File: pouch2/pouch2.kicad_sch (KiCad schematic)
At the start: 7 parts, among them U1 Pico

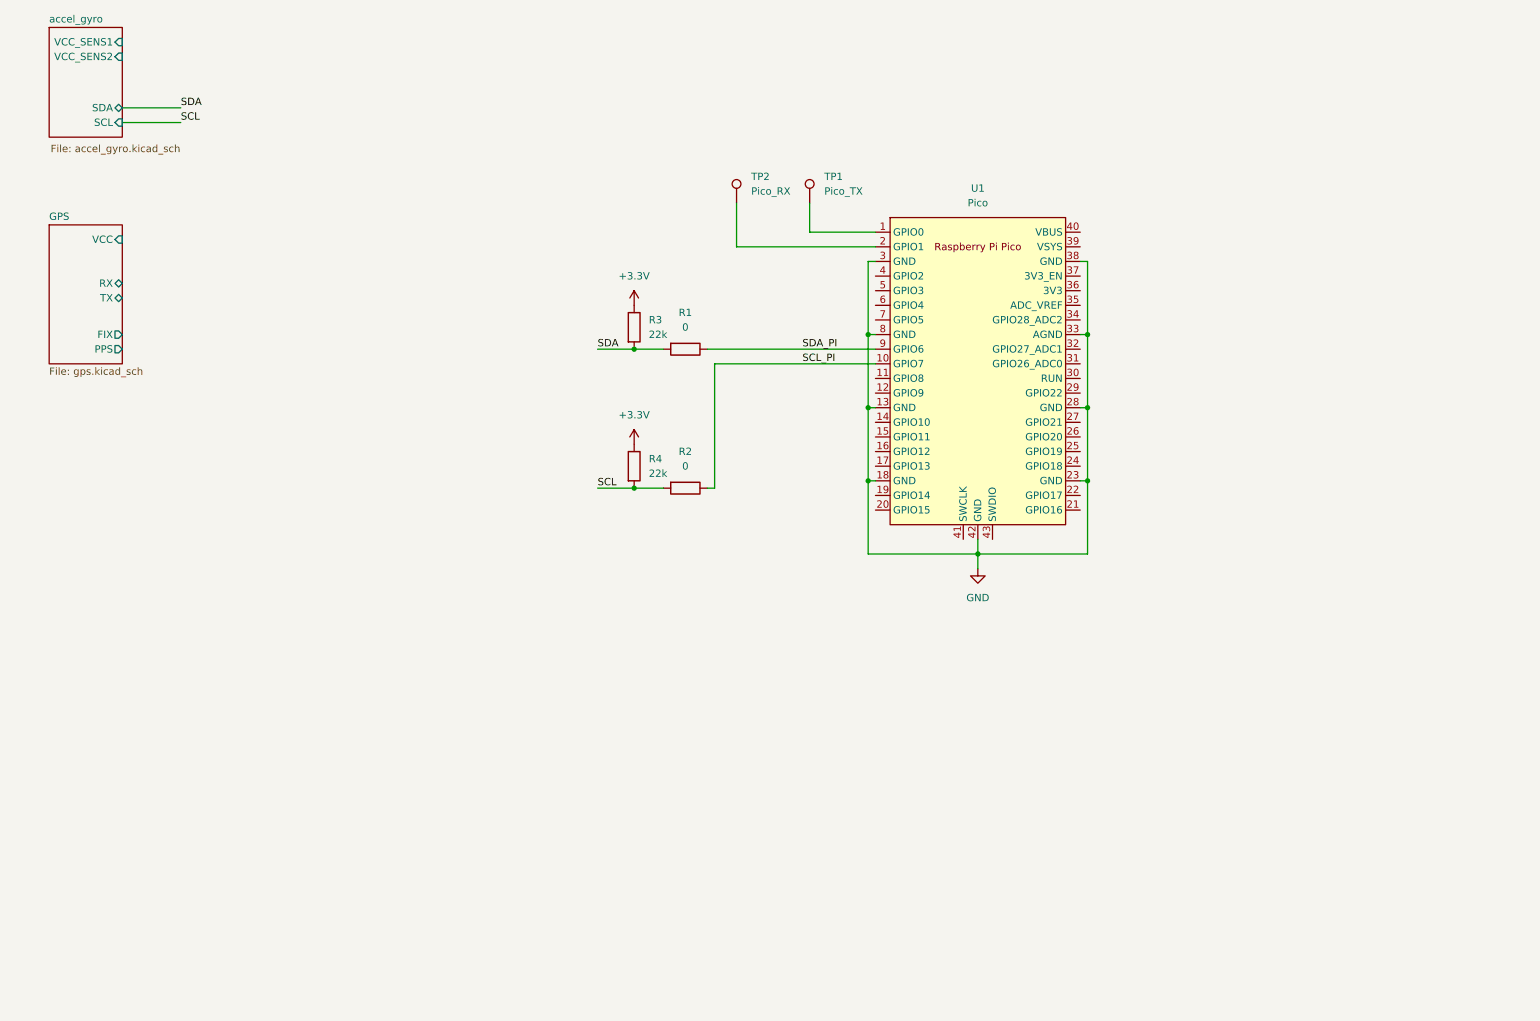
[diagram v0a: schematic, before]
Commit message: added power, sdcard
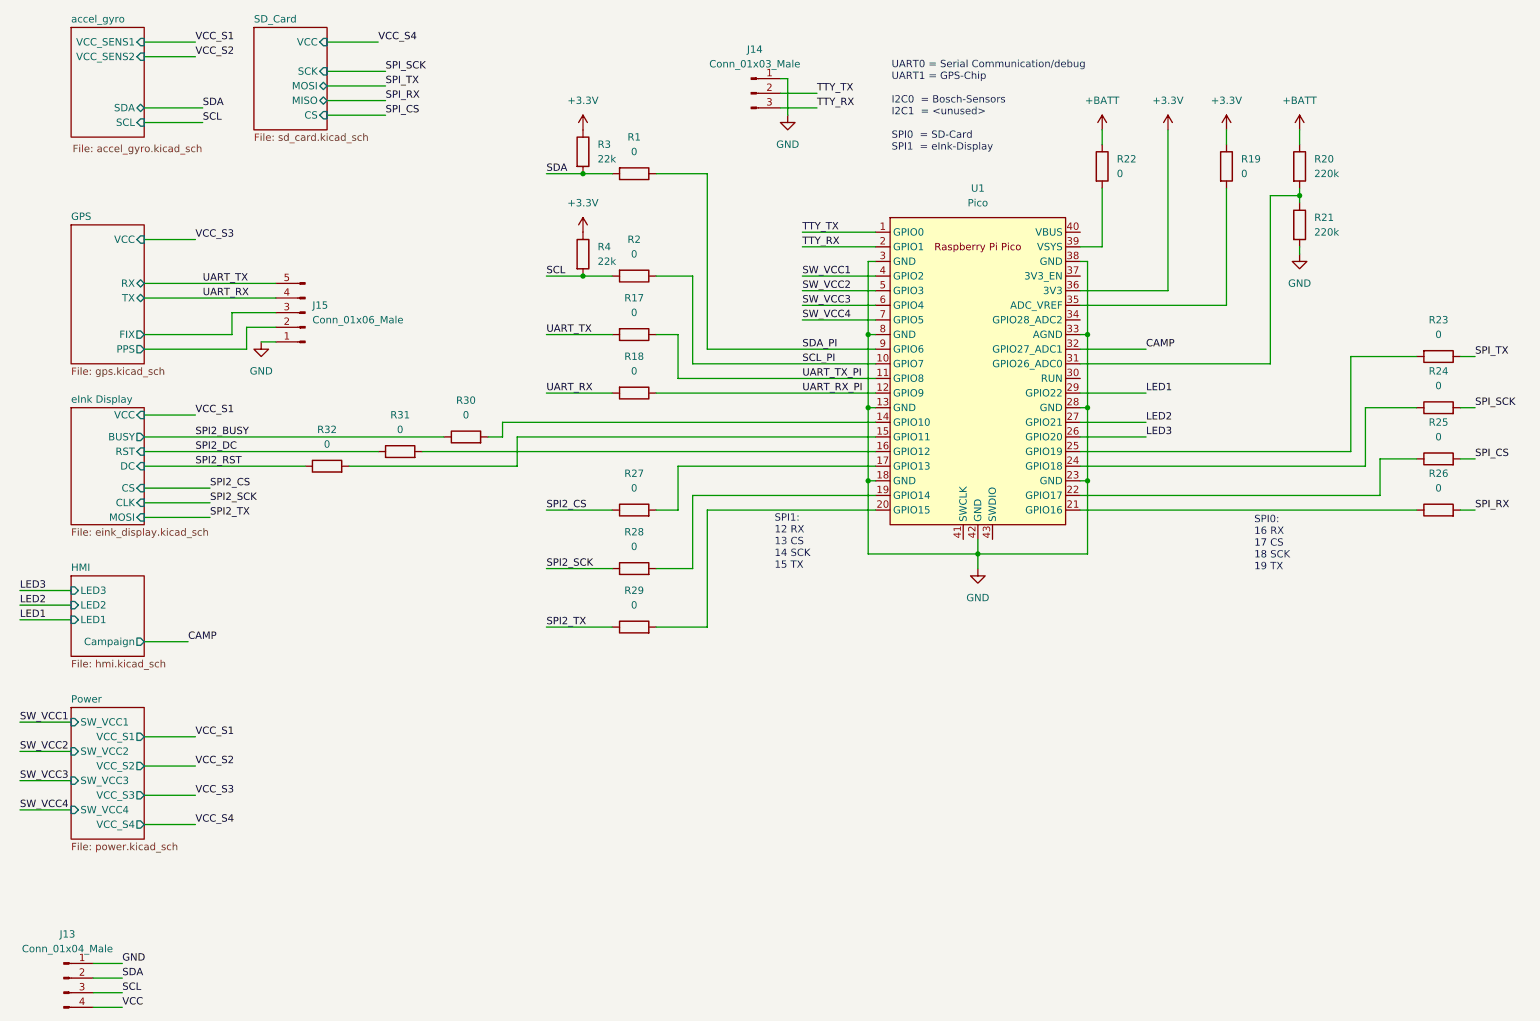
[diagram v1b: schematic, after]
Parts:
- removed TP1: Pico_TX, symbol Connector:TestPoint
- removed TP2: Pico_RX, symbol Connector:TestPoint
- added J13: Conn_01x04_Male, symbol Connector:Conn_01x04_Male
- added J14: Conn_01x03_Male, symbol Connector:Conn_01x03_Male
- added J15: Conn_01x06_Male, symbol Connector:Conn_01x05_Male
- added R17, R18, R19, R22, R23, R24, R25, R26, R27, R28, R29, R30, R31, R32: 0, symbol Device:R
- added R20, R21: 220k, symbol Device:R
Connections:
- net +3.3V: now also U1.36 (3V3), R19.1
- net GND: now also J13.1 (Pin_1), J14.1 (Pin_1), J15.1 (Pin_1), R21.2
- net GPS/FIX: now also J15.3 (Pin_3)
- net GPS/PPS: now also J15.2 (Pin_2)
- net SCL: now also J13.3 (Pin_3)
- net SDA: now also J13.2 (Pin_2)
- net TTY_RX: now reaches U1.2 (GPIO1)
- net TTY_RX: now also J14.3 (Pin_3)
- net TTY_TX: now reaches U1.1 (GPIO0)
- net TTY_TX: now also J14.2 (Pin_2)
- net UART_TX_PI: now reaches U1.11 (GPIO8)
- net UART_TX_PI: now also R17.1
- net UART_RX_PI: now reaches U1.12 (GPIO9)
- net UART_RX_PI: now also R18.1
- net at U1.14 (GPIO10): now also R30.2
- net at U1.15 (GPIO11): now also R32.2
- net at U1.16 (GPIO12): now also R31.2
- net at U1.17 (GPIO13): now also R27.2
- net at U1.19 (GPIO14): now also R28.2
- net at U1.20 (GPIO15): now also R29.2
- net at U1.21 (GPIO16): now also R26.1
- net at U1.22 (GPIO17): now also R25.1
- net at U1.24 (GPIO18): now also R24.1
- net at U1.25 (GPIO19): now also R23.2
- net LED3: now reaches U1.26 (GPIO20)
- net LED2: now reaches U1.27 (GPIO21)
- net LED1: now reaches U1.29 (GPIO22)
- net at U1.31 (GPIO26_ADC0): now also R20.2, R21.1
- net CAMP: now reaches U1.32 (GPIO27_ADC1)
- net at U1.35 (ADC_VREF): now also R19.2
- net at U1.39 (VSYS): now also R22.2
- net SW_VCC1: now reaches U1.4 (GPIO2)
- net SW_VCC2: now reaches U1.5 (GPIO3)
- net SW_VCC3: now reaches U1.6 (GPIO4)
- net SW_VCC4: now reaches U1.7 (GPIO5)
- new net +BATT: R20.1, R22.1
- new net SPI2_BUSY: R30.1
- new net SPI2_CS: R27.1
- new net SPI2_DC: R31.1
- new net SPI2_RST: R32.1
- new net SPI2_SCK: R28.1
- new net SPI2_TX: R29.1
- new net SPI_CS: R25.2
- new net SPI_RX: R26.2
- new net SPI_SCK: R24.2
- new net SPI_TX: R23.1
- new net UART_RX: J15.4 (Pin_4), R18.2
- new net UART_TX: J15.5 (Pin_5), R17.2
- new net VCC: J13.4 (Pin_4)
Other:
- added sheet HMI (hmi.kicad_sch)
- added sheet Power (power.kicad_sch)
- added sheet SD_Card (sd_card.kicad_sch)
- added sheet eInk Display (eink_display.kicad_sch)
- note added: "SPI0: 16 RX 17 CS 18 SCK 19 TX"
- note added: "SPI1: 12 RX 13 CS 14 SCK 15 TX"
- note added: "UART0 = Serial Communication/debug UART1 = GPS-Chip I2C0 = Bosch-Sensors I2C1 = <unused> SPI0 = SD-Card SPI1 = eInk-Display"
- moved on the sheet: R1, R2, R3, R4

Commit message: added pi zero header
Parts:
- J13: footprint (none) -> Connector_PinHeader_2.54mm:PinHeader_1x04_P2.54mm_Horizontal
- J14: footprint (none) -> Connector_PinHeader_2.54mm:PinHeader_1x03_P2.54mm_Horizontal
- J15: footprint (none) -> Connector_PinHeader_2.54mm:PinHeader_1x06_P2.54mm_Horizontal
- R1: footprint (none) -> Resistor_SMD:R_0805_2012Metric
- R17, R18, R19, R2, R20, R21, R22, R23, R24, R25, R26, R27, R28, R29, R3, R30, R31, R32, R4: footprint (none) -> Resistor_SMD:R_0815_2038Metric
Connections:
- net VCC is gone; now on net +3.3V: J13.4 (Pin_4)
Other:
- added sheet PiCoupler (pi_zero.kicad_sch)
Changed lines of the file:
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@@
-		)
-	)
-	(label "VCC"
-		(at 35.56 187.96 0)
-		(fields_autoplaced yes)
-		(effects
-			(font
-				(size 1.27 1.27)
-			)
-			(justify left bottom)
 		)
 	)
@@
 			)
 		)
-		(property "Footprint" ""
+		(property "Footprint" "Resistor_SMD:R_0815_2038Metric"
 			(at 264.16 94.488 90)
 			(effects
@@
 	)
 	(symbol
+		(lib_id "power:+3.3V")
+		(at 35.56 187.96 270)
+		(unit 1)
+		(exclude_from_sim no)
+		(in_bom yes)
+		(on_board yes)
+		(dnp no)
+		(fields_autoplaced yes)
+		(property "Reference" "#PWR033"
+			(at 31.75 187.96 0)
+			(effects
+				(font
+					(size 1.27 1.27)
+				)
+				(hide yes)
+			)
+		)
+		(property "Value" "+3.3V"
+			(at 39.37 187.9599 90)
+			(effects
+				(font
+					(size 1.27 1.27)
+				)
+				(justify left)
+			)
+		)
+		(property "Footprint" ""
+			(at 35.56 187.96 0)
+			(effects
+				(font
+					(size 1.27 1.27)
+				)
+				(hide yes)
+			)
+		)
+		(property "Datasheet" ""
+			(at 35.56 187.96 0)
+			(effects
+				(font
+					(size 1.27 1.27)
+				)
+				(hide yes)
+			)
+		)
+		(property "Description" "Power symbol creates a global label with name \"+3.3V\""
+			(at 35.56 187.96 0)
+			(effects
+				(font
+					(size 1.27 1.27)
+				)
+				(hide yes)
+			)
+		)
+		(pin "1"
+		)
+		(instances
+			(project ""
+				(path "/278cfa6b-9496-4a22-b425-8abdb96793ef"
+					(reference "#PWR033")
+					(unit 1)
+				)
+			)
+		)
+	)
+	(symbol
 		(lib_id "Device:R")
 		(at 240.03 41.91 0)
@@
 			)
 		)
-		(property "Footprint" ""
+		(property "Footprint" "Resistor_SMD:R_0815_2038Metric"
 			(at 238.252 41.91 90)
 			(effects
@@
 			)
 		)
-		(property "Footprint" ""
+		(property "Footprint" "Resistor_SMD:R_0815_2038Metric"
 			(at 124.46 103.378 90)
 			(effects
@@
 			)
 		)
-		(property "Footprint" ""
+		(property "Footprint" "Resistor_SMD:R_0815_2038Metric"
 			(at 124.46 59.182 90)
 			(effects
@@
 			)
 		)
-		(property "Footprint" ""
+		(property "Footprint" "Connector_PinHeader_2.54mm:PinHeader_1x06_P2.54mm_Horizontal"
 			(at 67.31 67.31 0)
 			(effects
@@
 			)
 		)
-		(property "Footprint" ""
+		(property "Footprint" "Resistor_SMD:R_0815_2038Metric"
 			(at 124.46 79.502 90)
 			(effects
@@
 			)
 		)
-		(property "Footprint" ""
+		(property "Footprint" "Resistor_SMD:R_0815_2038Metric"
 			(at 113.792 39.37 90)
 			(effects
@@
 			)
 		)
-		(property "Footprint" ""
+		(property "Footprint" "Connector_PinHeader_2.54mm:PinHeader_1x04_P2.54mm_Horizontal"
 			(at 25.4 182.88 0)
 			(effects
@@
 			)
 		)
-		(property "Footprint" ""
+		(property "Footprint" "Resistor_SMD:R_0815_2038Metric"
 			(at 264.16 85.598 90)
 			(effects
@@
 			)
 		)
-		(property "Footprint" ""
+		(property "Footprint" "Connector_PinHeader_2.54mm:PinHeader_1x03_P2.54mm_Horizontal"
 			(at 144.78 29.21 0)
 			(effects
@@
 			)
 		)
-		(property "Footprint" ""
+		(property "Footprint" "Resistor_SMD:R_0815_2038Metric"
 			(at 264.16 73.152 90)
 			(effects
@@
 			)
 		)
-		(property "Footprint" ""
+		(property "Footprint" "Resistor_SMD:R_0815_2038Metric"
 			(at 225.552 41.91 90)
 			(effects
@@
 			)
 		)
-		(property "Footprint" ""
+		(property "Footprint" "Resistor_SMD:R_0805_2012Metric"
 			(at 124.46 41.402 90)
 			(effects
@@
 			)
 		)
-		(property "Footprint" ""
+		(property "Footprint" "Resistor_SMD:R_0815_2038Metric"
 			(at 124.46 113.538 90)
 			(effects
@@
 			)
 		)
-		(property "Footprint" ""
+		(property "Footprint" "Resistor_SMD:R_0815_2038Metric"
 			(at 203.962 41.91 90)
 			(effects
@@
 			)
 		)
-		(property "Footprint" ""
+		(property "Footprint" "Resistor_SMD:R_0815_2038Metric"
 			(at 83.82 93.218 90)
 			(effects
@@
 			)
 		)
-		(property "Footprint" ""
+		(property "Footprint" "Resistor_SMD:R_0815_2038Metric"
 			(at 71.12 95.758 90)
 			(effects
@@
 			)
 		)
-		(property "Footprint" ""
+		(property "Footprint" "Resistor_SMD:R_0815_2038Metric"
 			(at 95.25 90.678 90)
 			(effects
@@
 			)
 		)
-		(property "Footprint" ""
+		(property "Footprint" "Resistor_SMD:R_0815_2038Metric"
 			(at 238.252 52.07 90)
 			(effects
@@
 			)
 		)
-		(property "Footprint" ""
+		(property "Footprint" "Resistor_SMD:R_0815_2038Metric"
 			(at 113.792 57.15 90)
 			(effects
@@
 			)
 		)
-		(property "Footprint" ""
+		(property "Footprint" "Resistor_SMD:R_0815_2038Metric"
 			(at 264.16 103.378 90)
 			(effects
@@
 			)
 		)
-		(property "Footprint" ""
+		(property "Footprint" "Resistor_SMD:R_0815_2038Metric"
 			(at 124.46 123.698 90)
 			(effects
@@
 			)
 		)
-		(property "Footprint" ""
+		(property "Footprint" "Resistor_SMD:R_0815_2038Metric"
 			(at 124.46 69.342 90)
 			(effects
@@
 				)
 			)
+		)
+	)
+	(sheet
+		(at 59.69 172.72)
+		(size 15.24 16.51)
+		(fields_autoplaced yes)
+		(stroke
+			(width 0.1524)
+			(type solid)
+		)
+		(fill
+			(color 0 0 0 0.0000)
+		)
+		(property "Sheetname" "PiCoupler"
+			(at 59.69 172.0084 0)
+			(effects
+				(font
+					(size 1.27 1.27)
+				)
+				(justify left bottom)
+			)
+		)
+		(property "Sheetfile" "pi_zero.kicad_sch"
+			(at 59.69 189.8146 0)
+			(effects
+				(font
+					(size 1.27 1.27)
+				)
+				(justify left top)
+			)
+		)
+		(pin "POWERON" input
+			(at 59.69 177.8 180)
+			(effects
+				(font
+					(size 1.27 1.27)
+				)
+				(justify left)
+			)
+		)
+		(pin "READY" output
+			(at 74.93 180.34 0)
+			(effects
+				(font
+					(size 1.27 1.27)
+				)
+				(justify right)
+			)
+		)
+		(pin "SDA" output
+			(at 74.93 184.15 0)
+			(effects
+				(font
+					(size 1.27 1.27)
+				)
+				(justify right)
+			)
+		)
+		(pin "SCL" input
+			(at 74.93 186.69 0)
+			(effects
+				(font
+					(size 1.27 1.27)
+				)
+				(justify right)
+			)
+		)
+		(pin "PI_VCC" input
+			(at 59.69 175.26 180)
+			(effects
+				(font
+					(size 1.27 1.27)
+				)
+				(justify left)
+			)
+		)
+		(instances
+			(project "pouch2"
+				(path "/278cfa6b-9496-4a22-b425-8abdb96793ef"
+					(page "8")
+				)
+			)

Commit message: started PCB design
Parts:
- J101: renamed from J13; footprint Connector_PinHeader_2.54mm:PinHeader_1x04_P2.54mm_Horizontal -> Connector_PinHeader_2.54mm:PinHeader_1x04_P2.54mm_Vertical
- J102: renamed from J15; footprint Connector_PinHeader_2.54mm:PinHeader_1x06_P2.54mm_Horizontal -> Connector_PinHeader_2.54mm:PinHeader_1x06_P2.54mm_Vertical
- J103: renamed from J14; footprint Connector_PinHeader_2.54mm:PinHeader_1x03_P2.54mm_Horizontal -> Connector_PinHeader_2.54mm:PinHeader_1x03_P2.54mm_Vertical
- R101: renamed from R32; footprint Resistor_SMD:R_0815_2038Metric -> Resistor_SMD:R_0805_2012Metric
- R102: renamed from R31; footprint Resistor_SMD:R_0815_2038Metric -> Resistor_SMD:R_0805_2012Metric
- R103: renamed from R30; footprint Resistor_SMD:R_0815_2038Metric -> Resistor_SMD:R_0805_2012Metric
- R104: renamed from R3; footprint Resistor_SMD:R_0815_2038Metric -> Resistor_SMD:R_0805_2012Metric
- R105: renamed from R4; footprint Resistor_SMD:R_0815_2038Metric -> Resistor_SMD:R_0805_2012Metric
- R107: renamed from R2; footprint Resistor_SMD:R_0815_2038Metric -> Resistor_SMD:R_0805_2012Metric
- R108: renamed from R17; footprint Resistor_SMD:R_0815_2038Metric -> Resistor_SMD:R_0805_2012Metric
- R109: renamed from R18; footprint Resistor_SMD:R_0815_2038Metric -> Resistor_SMD:R_0805_2012Metric
- R110: renamed from R27; footprint Resistor_SMD:R_0815_2038Metric -> Resistor_SMD:R_0805_2012Metric
- R111: renamed from R28; footprint Resistor_SMD:R_0815_2038Metric -> Resistor_SMD:R_0805_2012Metric
- R112: renamed from R29; footprint Resistor_SMD:R_0815_2038Metric -> Resistor_SMD:R_0805_2012Metric
- R113: renamed from R22; footprint Resistor_SMD:R_0815_2038Metric -> Resistor_SMD:R_0805_2012Metric
- R114: renamed from R19; footprint Resistor_SMD:R_0815_2038Metric -> Resistor_SMD:R_0805_2012Metric
- R115: renamed from R20; footprint Resistor_SMD:R_0815_2038Metric -> Resistor_SMD:R_0805_2012Metric
- R116: renamed from R21; footprint Resistor_SMD:R_0815_2038Metric -> Resistor_SMD:R_0805_2012Metric
- R117: renamed from R23; footprint Resistor_SMD:R_0815_2038Metric -> Resistor_SMD:R_0805_2012Metric
- R118: renamed from R24; footprint Resistor_SMD:R_0815_2038Metric -> Resistor_SMD:R_0805_2012Metric
- R119: renamed from R25; footprint Resistor_SMD:R_0815_2038Metric -> Resistor_SMD:R_0805_2012Metric
- R120: renamed from R26; footprint Resistor_SMD:R_0815_2038Metric -> Resistor_SMD:R_0805_2012Metric
- U101: renamed from U1; footprint RPi_Pico:RPi_Pico_SMD_TH -> MCU_RaspberryPi_and_Boards:RPi_Pico_SMD_TH
- renumbered R1 to R106

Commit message: PCB and footprint arrangements
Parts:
- added H101, H102, H103, H104: MountingHole, MountingHole:MountingHole_3.2mm_M3_DIN965_Pad_TopBottom, symbol Mechanical:MountingHole

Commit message: added SIM 868 schematic
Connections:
- net SPI2_CS: no longer R110.1
- new net SPI2_CS_SD: R110.1
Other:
- sheet SD_Card renamed SD Card
- sheet accel_gyro renamed Accelerometer, Gyroscope
- added sheet SIM (sim868_module.kicad_sch)
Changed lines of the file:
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@@
 	(generator "eeschema")
 	(generator_version "8.0")
-	(paper "A4")
+	(paper "A3")
 	(title_block
 		(title "Pouch 2")
@@
 		)
 	)
-	(label "SPI2_CS"
+	(label "SPI2_CS_SD"
 		(at 109.22 101.6 0)
 		(fields_autoplaced yes)
@@
 		)
 	)
-	(label "SPI_CS"
+	(label "SPI_CS_SD"
 		(at 81.28 33.02 0)
 		(fields_autoplaced yes)
@@
 			(color 0 0 0 0.0000)
 		)
-		(property "Sheetname" "accel_gyro"
+		(property "Sheetname" "Accelerometer, Gyroscope"
 			(at 26.67 17.0684 0)
 			(effects
@@
 			(color 0 0 0 0.0000)
 		)
-		(property "Sheetname" "SD_Card"
+		(property "Sheetname" "SD Card"
 			(at 58.42 17.0684 0)
 			(effects
@@
 				)
 			)
+		)
+	)
+	(sheet
+		(at 27.94 200.66)
+		(size 20.32 25.4)
+		(fields_autoplaced yes)
+		(stroke
+			(width 0.1524)
+			(type solid)
+		)
+		(fill
+			(color 0 0 0 0.0000)
+		)
+		(property "Sheetname" "SIM"
+			(at 27.94 199.9484 0)
+			(effects
+				(font
+					(size 1.27 1.27)
+				)
+				(justify left bottom)
+			)
+		)
+		(property "Sheetfile" "sim868_module.kicad_sch"
+			(at 27.94 226.6446 0)
+			(effects
+				(font
+					(size 1.27 1.27)
+				)
+				(justify left top)
+			)
+		)
+		(instances
+			(project "pouch2"
+				(path "/278cfa6b-9496-4a22-b425-8abdb96793ef"
+					(page "9")
+				)
+			)

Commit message: started routing
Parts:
- added R121: 0, Resistor_SMD:R_0805_2012Metric, symbol Device:R
- J102: footprint Connector_PinHeader_2.54mm:PinHeader_1x06_P2.54mm_Vertical -> Connector_PinHeader_2.54mm:PinHeader_1x05_P2.54mm_Vertical
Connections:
- net GPS/FIX is gone; now on net UART_RX: J102.3 (Pin_3)
- net GPS/PPS is gone; now on net UART_TX: J102.2 (Pin_2)
- net SPI2_CS_SD is gone; now on net SPI2_CS: R110.1
- net SPI_CS is gone; now on net SPI_CS_SD: R119.2
- net +3.3V: now also R121.1; no longer U101.36 (3V3)
- net UART_RX: no longer J102.4 (Pin_4)
- net UART_TX: no longer J102.5 (Pin_5)
- net PI_SPI0_CS: now reaches R119.1, U101.22 (GPIO17)
- net PI_SPI0_SCK: now reaches R118.1, U101.24 (GPIO18)
- net PI_SPI0_RX: now reaches R120.1, U101.21 (GPIO16)
- net PI_SPI0_TX: now reaches R117.2, U101.25 (GPIO19)
- net SCL_PI renamed PI_I2C0_SCL
- net SDA_PI renamed PI_I2C0_SDA
- net SPI2_BUSY renamed DISP_BUSY
- net SPI2_DC renamed DISP_DC
- net SPI2_RST renamed DISP_RST
- net UART_RX_PI renamed PI_UART0_RX
- net UART_TX_PI renamed PI_UART0_TX
- new net: R121.2, U101.36 (3V3)
- new net GPS_FIX: J102.4 (Pin_4)
- new net GPS_PPS: J102.5 (Pin_5)
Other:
- note added: "SPI1: 12 RX (DC) 13 CS 14 SCK 15 TX"
- note removed: "SPI1: 12 RX 13 CS 14 SCK 15 TX"
- moved on the sheet: H101, H102, H103, H104, J101, J103, R101, R102, R103, R104, R105, R106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

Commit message: drawed a lot of things
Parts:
- renumbered J102 to J101, J103 to J102, J101 to J103, R104 to R101, R105 to R102, R106 to R103, R107 to R104, R108 to R105, R109 to R106, R103 to R107, R101 to R108, R102 to R109, R121 to R114, R114 to R115, R115 to R116, R116 to R117, R117 to R118, R118 to R119, R119 to R120, R120 to R121
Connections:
- net CPU_READY: now reaches U101.34 (GPIO28_ADC2)
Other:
- sheet Power ports: added VCC_S5, VCC_S6, VCC_S7, VCC_S8; removed none
- note added: "I2C0"
- note added: "Power rails S1 = Bosch-Sensors S2 = Gyroscope S3 = GPS S4 = SD-Card S5 = E-Ink-Display S6 = S7 = SIM-Module S8 = Pi-Zero"
- note added: "UART0"
- note added: "UART1"
